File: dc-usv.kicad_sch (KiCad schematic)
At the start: 0 parts

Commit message: Partial layout
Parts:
- added CASE1: 1455L1601, Case:1455L1601, symbol Case:1455L1601
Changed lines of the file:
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@@
+    )
+  )
+  (symbol (lib_id "Case:1455L1601") (at 20.32 35.56 0) (unit 1)
+    (in_bom yes) (on_board yes) (fields_autoplaced)
+    (property "Reference" "CASE1" (id 0) (at 20.32 30.7172 0))
+    (property "Value" "1455L1601" (id 1) (at 20.32 33.2541 0))
+    (property "Footprint" "Case:1455L1601" (id 2) (at 20.32 35.56 0)
+      (effects (font (size 1.27 1.27)) hide)
+    )
+    (property "Datasheet" "https://cdn-reichelt.de/documents/datenblatt/C700/1455L1601.pdf" (id 3) (at 20.32 35.56 0)
+      (effects (font (size 1.27 1.27)) hide)
     )
   )
@@
       (reference "#PWR0216") (unit 1) (value "GND") (footprint "")
     )
-    (path "/a06395f1-7afb-45e9-b1be-eb1d60bae674/01dae7e9-d4e0-426e-b265-29ae7f554ffd"
-      (reference "#PWR0217") (unit 1) (value "+3.3V") (footprint "")
+    (path "/a06395f1-7afb-45e9-b1be-eb1d60bae674/0ccfaabc-1cfb-4d04-b197-585448db4bdb"
+      (reference "#PWR0217") (unit 1) (value "+3V3") (footprint "")
     )
     (path "/a06395f1-7afb-45e9-b1be-eb1d60bae674/9b461fb2-d53a-4d81-9704-1a7841368fff"
@@
       (reference "#PWR0296") (unit 1) (value "+3V3") (footprint "")
     )
+    (path "/a06395f1-7afb-45e9-b1be-eb1d60bae674/53a3dabf-d840-40d3-b123-be99bc0cd47b"
+      (reference "#PWR0297") (unit 1) (value "+3V3") (footprint "")
+    )
+    (path "/a06395f1-7afb-45e9-b1be-eb1d60bae674/b7e85537-781d-41e1-bbe8-d28bedf5aecc"
+      (reference "#PWR0298") (unit 1) (value "GND") (footprint "")
+    )
     (path "/a06395f1-7afb-45e9-b1be-eb1d60bae674/0ede46ea-4de7-4fa6-810f-0ba49bf63961"
-      (reference "#PWR?") (unit 1) (value "GND") (footprint "")
-    )
-    (path "/a06395f1-7afb-45e9-b1be-eb1d60bae674/53a3dabf-d840-40d3-b123-be99bc0cd47b"
-      (reference "#PWR?") (unit 1) (value "+3V3") (footprint "")
-    )
-    (path "/a06395f1-7afb-45e9-b1be-eb1d60bae674/b7e85537-781d-41e1-bbe8-d28bedf5aecc"
-      (reference "#PWR?") (unit 1) (value "GND") (footprint "")
+      (reference "#PWR0299") (unit 1) (value "GND") (footprint "")
+    )
+    (path "/9f5e79bf-a1ad-420a-9a06-1a81ab265187/9868f416-b036-4007-b8a7-93d9fd668084"
+      (reference "#PWR0300") (unit 1) (value "GND") (footprint "")
+    )
+    (path "/9f5e79bf-a1ad-420a-9a06-1a81ab265187/c7c0a035-6c4c-4ca1-80e7-b1a325e95302"
+      (reference "#PWR0301") (unit 1) (value "+3V3") (footprint "")
+    )
+    (path "/9f5e79bf-a1ad-420a-9a06-1a81ab265187/93b8629d-2dd9-48b6-a0a5-986d19c60970"
+      (reference "#PWR0302") (unit 1) (value "GND") (footprint "")
+    )
+    (path "/9f5e79bf-a1ad-420a-9a06-1a81ab265187/9e16cf65-2ec4-4650-b1d7-fd409aef4ec7"
+      (reference "#PWR0303") (unit 1) (value "GND") (footprint "")
+    )
+    (path "/9f5e79bf-a1ad-420a-9a06-1a81ab265187/289a5c1c-0bf1-4333-b01f-9d95e3fa2864"
+      (reference "#PWR0304") (unit 1) (value "GND") (footprint "")
+    )
+    (path "/a06395f1-7afb-45e9-b1be-eb1d60bae674/b2d83311-3769-443b-9605-bbef8899a620/89f70569-72d2-4912-b6e3-9703a730d568"
+      (reference "#PWR0305") (unit 1) (value "VBUS") (footprint "")
+    )
+    (path "/a06395f1-7afb-45e9-b1be-eb1d60bae674/b2d83311-3769-443b-9605-bbef8899a620/9f2c905a-ca7b-475b-8632-d31e68011e41"
+      (reference "#PWR0306") (unit 1) (value "GND") (footprint "")
     )
     (path "/aa145c2f-e167-4de3-92bf-3e0d0ae2fb67/06ec14b7-6af4-46b3-aed4-1258a100ed19"
@@
       (reference "C103") (unit 1) (value "2.2uF") (footprint "Capacitor_SMD:C_0603_1608Metric")
     )
+    (path "/9f5e79bf-a1ad-420a-9a06-1a81ab265187/88747cb4-c96e-48fe-8bd4-16f22b505b73"
+      (reference "C104") (unit 1) (value "22nF") (footprint "Capacitor_SMD:C_0402_1005Metric")
+    )
+    (path "/25526d58-38a0-4dab-a440-f8cc76091337"
+      (reference "CASE1") (unit 1) (value "1455L1601") (footprint "Case:1455L1601")
+    )
     (path "/aa145c2f-e167-4de3-92bf-3e0d0ae2fb67/defc8839-bf1e-4b04-89fc-3cffafd43258"
       (reference "D1") (unit 1) (value "1N4148WS") (footprint "Diode_SMD:D_SOD-323")
@@
       (reference "D16") (unit 1) (value "P6SMB6.8CA") (footprint "Diode_SMD:D_SMB")
     )
+    (path "/9f5e79bf-a1ad-420a-9a06-1a81ab265187/81f255d2-fff4-4286-9b04-e2b96723db7d"
+      (reference "D17") (unit 1) (value "YEL") (footprint "LED_SMD:LED_0603_1608Metric")
+    )
+    (path "/9f5e79bf-a1ad-420a-9a06-1a81ab265187/c68b69ec-7a92-49e2-b6d4-229cddc59a1a"
+      (reference "D18") (unit 1) (value "RED") (footprint "LED_SMD:LED_0603_1608Metric")
+    )
+    (path "/9f5e79bf-a1ad-420a-9a06-1a81ab265187/e64f1ef4-0563-4bae-a757-db5967d3b8e2"
+      (reference "D19") (unit 1) (value "GRN") (footprint "LED_SMD:LED_0603_1608Metric")
+    )
     (path "/aa145c2f-e167-4de3-92bf-3e0d0ae2fb67/a0a04842-0b26-4142-b5e1-0b95e4dc5d49"
       (reference "F1") (unit 1) (value "10A") (footprint "Fuse:Fuse_1206_3216Metric")
@@
       (reference "Q25") (unit 1) (value "AO3401A") (footprint "Package_TO_SOT_SMD:SOT-23")
     )
+    (path "/9f5e79bf-a1ad-420a-9a06-1a81ab265187/6c3c82b9-4c87-4dcf-ad4d-ca684d7318df"
+      (reference "Q26") (unit 1) (value "2N7002") (footprint "Package_TO_SOT_SMD:SOT-23")
+    )
     (path "/a06395f1-7afb-45e9-b1be-eb1d60bae674/b2d83311-3769-443b-9605-bbef8899a620/0b0d926e-5c20-493a-95ff-4ae891ae05a1"
       (reference "Q28") (unit 1) (value "MMBT3904") (footprint "Package_TO_SOT_SMD:SOT-23")
@@
     )
     (path "/a06395f1-7afb-45e9-b1be-eb1d60bae674/59d225b3-da12-45b8-9dfd-44678b17239f"
-      (reference "R?") (unit 1) (value "10k") (footprint "Resistor_SMD:R_0402_1005Metric")
+      (reference "R118") (unit 1) (value "10k") (footprint "Resistor_SMD:R_0402_1005Metric")
+    )
+    (path "/9f5e79bf-a1ad-420a-9a06-1a81ab265187/4a912a3f-fccf-4f23-9667-38ea759c76bf"
+      (reference "R119") (unit 1) (value "10k") (footprint "Resistor_SMD:R_0402_1005Metric")
+    )
+    (path "/9f5e79bf-a1ad-420a-9a06-1a81ab265187/f4357ab5-8e36-423b-add8-f1b628003a7c"
+      (reference "R120") (unit 1) (value "5.1k") (footprint "Resistor_SMD:R_0402_1005Metric")
+    )
+    (path "/9f5e79bf-a1ad-420a-9a06-1a81ab265187/0eca0453-18ac-4661-a9b1-51916678fe1b"
+      (reference "R121") (unit 1) (value "10k") (footprint "Resistor_SMD:R_0402_1005Metric")
     )
     (path "/4ce9e4d8-553f-40e6-a397-66d04db306f8/3152910b-dfc7-4fc7-87ab-336be9ca10d0"
@@
     )
     (path "/a06395f1-7afb-45e9-b1be-eb1d60bae674/e6846060-390f-4c53-9367-e476d0b72950"
-      (reference "SW?") (unit 1) (value "SW_Push") (footprint "Button_Switch_SMD_LCSC:x-1825027-x")
+      (reference "SW2") (unit 1) (value "SW_Push") (footprint "Button_Switch_SMD_LCSC:x-1825027-x")
     )
     (path "/aa145c2f-e167-4de3-92bf-3e0d0ae2fb67/d6dc2035-6098-4e26-82f4-b5badac60c84"
-      (reference "TH1") (unit 1) (value "10k") (footprint "Resistor_SMD:R_0805_2012Metric")
+      (reference "TH1") (unit 1) (value "10k") (footprint "Resistor_SMD:R_0402_1005Metric")
     )
     (path "/aa145c2f-e167-4de3-92bf-3e0d0ae2fb67/4006ff34-ec5f-4578-a6c2-03607b44d972"
-      (reference "TH2") (unit 1) (value "10k") (footprint "Resistor_SMD:R_0805_2012Metric")
+      (reference "TH2") (unit 1) (value "10k") (footprint "Resistor_SMD:R_0402_1005Metric")
     )
     (path "/aa145c2f-e167-4de3-92bf-3e0d0ae2fb67/287ca5de-cbb9-4736-9b09-b0aab9fee0e6"
@@
       (reference "U17") (unit 1) (value "N066-6448TSWEG03-H28") (footprint "Display_OLED:N066-6448TSWEG03-H28")
     )
+    (path "/a06395f1-7afb-45e9-b1be-eb1d60bae674/b2d83311-3769-443b-9605-bbef8899a620/3f24a504-1454-471f-9aa3-b57372c43cf7"
+      (reference "U18") (unit 1) (value "SRV05-4") (footprint "Package_TO_SOT_SMD:SOT-23-6")
+    )
     (path "/a06395f1-7afb-45e9-b1be-eb1d60bae674/b2d83311-3769-443b-9605-bbef8899a620/c8035e2e-1a39-416d-bfe6-a3df66d2a4a2"

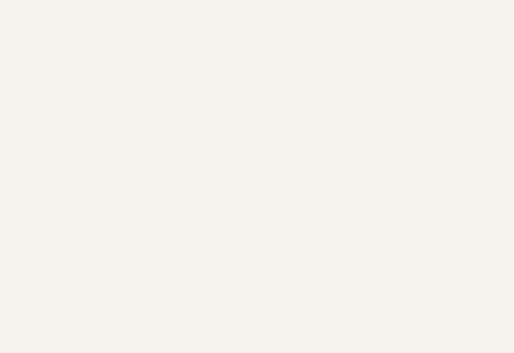
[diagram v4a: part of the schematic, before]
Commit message: Add tooling holes
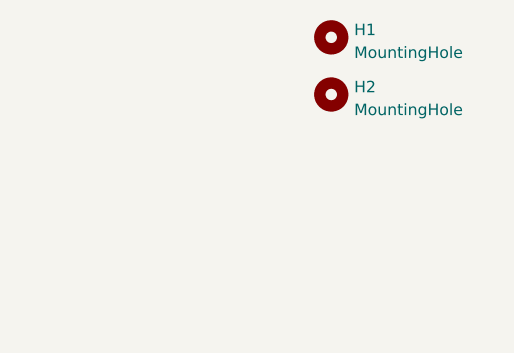
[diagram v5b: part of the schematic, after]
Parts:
- added H1, H2: MountingHole, ToolingHole:ToolingHole_JLCSMT, symbol Mechanical:MountingHole
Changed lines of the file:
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@@
+    )
+  )
+  (symbol (lib_id "Mechanical:MountingHole") (at 267.97 15.24 0) (unit 1)
+    (in_bom no) (on_board yes) (fields_autoplaced)
+    (property "Reference" "H1" (id 0) (at 270.51 14.4053 0)
+      (effects (font (size 1.27 1.27)) (justify left))
+    )
+    (property "Value" "MountingHole" (id 1) (at 270.51 16.9422 0)
+      (effects (font (size 1.27 1.27)) (justify left))
+    )
+    (property "Footprint" "ToolingHole:ToolingHole_JLCSMT" (id 2) (at 267.97 15.24 0)
+      (effects (font (size 1.27 1.27)) hide)
+    )
+    (property "Datasheet" "~" (id 3) (at 267.97 15.24 0)
+      (effects (font (size 1.27 1.27)) hide)
+    )
+  )
+  (symbol (lib_id "Mechanical:MountingHole") (at 267.97 21.59 0) (unit 1)
+    (in_bom no) (on_board yes) (fields_autoplaced)
+    (property "Reference" "H2" (id 0) (at 270.51 20.7553 0)
+      (effects (font (size 1.27 1.27)) (justify left))
+    )
+    (property "Value" "MountingHole" (id 1) (at 270.51 23.2922 0)
+      (effects (font (size 1.27 1.27)) (justify left))
+    )
+    (property "Footprint" "ToolingHole:ToolingHole_JLCSMT" (id 2) (at 267.97 21.59 0)
+      (effects (font (size 1.27 1.27)) hide)
+    )
+    (property "Datasheet" "~" (id 3) (at 267.97 21.59 0)
+      (effects (font (size 1.27 1.27)) hide)
     )
   )
@@
       (reference "F4") (unit 1) (value "5A") (footprint "Fuse:Fuse_1206_3216Metric")
     )
+    (path "/b1de0cf0-daa1-4d20-a7d3-2194d7487162"
+      (reference "H1") (unit 1) (value "MountingHole") (footprint "ToolingHole:ToolingHole_JLCSMT")
+    )
+    (path "/fdcbfa9b-5014-4601-9d27-0786e14eb279"
+      (reference "H2") (unit 1) (value "MountingHole") (footprint "ToolingHole:ToolingHole_JLCSMT")
+    )
     (path "/ba11ff08-fab3-423b-91ea-f3fea9b2bab0/c29f14bf-2136-45fb-8c2b-3167cf235adb"

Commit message: Fix footprint origins for JLC assembly
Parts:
- CASE1: now left out of the parts list
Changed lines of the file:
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@@
   )
   (symbol (lib_id "Case:1455L1601") (at 20.32 35.56 0) (unit 1)
-    (in_bom yes) (on_board yes) (fields_autoplaced)
+    (in_bom no) (on_board yes) (fields_autoplaced)
     (property "Reference" "CASE1" (id 0) (at 20.32 30.7172 0))
     (property "Value" "1455L1601" (id 1) (at 20.32 33.2541 0))
@@
       (reference "#PWR0311") (unit 1) (value "+3V3") (footprint "")
     )
+    (path "/a06395f1-7afb-45e9-b1be-eb1d60bae674/c5b7f9e4-5132-4040-87a3-40d796a53fc8"
+      (reference "#PWR0312") (unit 1) (value "GND") (footprint "")
+    )
     (path "/a06395f1-7afb-45e9-b1be-eb1d60bae674/9ac33f4a-daa8-4947-b60b-5dc5ce181da9"
-      (reference "#PWR?") (unit 1) (value "GND") (footprint "")
+      (reference "#PWR0313") (unit 1) (value "GND") (footprint "")
     )
     (path "/db902e67-672f-4e23-a96d-1719af2dd4ad/c33dcca6-4622-478c-83f2-1aea854be53c"
-      (reference "#PWR?") (unit 1) (value "GND") (footprint "")
-    )
-    (path "/a06395f1-7afb-45e9-b1be-eb1d60bae674/c5b7f9e4-5132-4040-87a3-40d796a53fc8"
-      (reference "#PWR?") (unit 1) (value "GND") (footprint "")
+      (reference "#PWR0314") (unit 1) (value "GND") (footprint "")
     )
     (path "/aa145c2f-e167-4de3-92bf-3e0d0ae2fb67/06ec14b7-6af4-46b3-aed4-1258a100ed19"
@@
     )
     (path "/a06395f1-7afb-45e9-b1be-eb1d60bae674/9a721ec3-8301-444f-9eaa-aa53e11a19f3"
-      (reference "D?") (unit 1) (value "GRN") (footprint "LED_SMD:LED_0603_1608Metric")
+      (reference "D20") (unit 1) (value "GRN") (footprint "LED_SMD:LED_0603_1608Metric")
+    )
+    (path "/a06395f1-7afb-45e9-b1be-eb1d60bae674/ba96cd70-0d01-4998-b7c4-a03709754f62"
+      (reference "D21") (unit 1) (value "YEL") (footprint "LED_SMD:LED_0603_1608Metric")
     )
     (path "/db902e67-672f-4e23-a96d-1719af2dd4ad/b9897c5f-9291-4dbc-baca-8ebe9f116bad"
-      (reference "D?") (unit 1) (value "RED") (footprint "LED_SMD:LED_0603_1608Metric")
-    )
-    (path "/a06395f1-7afb-45e9-b1be-eb1d60bae674/ba96cd70-0d01-4998-b7c4-a03709754f62"
-      (reference "D?") (unit 1) (value "YEL") (footprint "LED_SMD:LED_0603_1608Metric")
+      (reference "D22") (unit 1) (value "RED") (footprint "LED_SMD:LED_0603_1608Metric")
     )
     (path "/aa145c2f-e167-4de3-92bf-3e0d0ae2fb67/a0a04842-0b26-4142-b5e1-0b95e4dc5d49"
@@
       (reference "R123") (unit 1) (value "100R") (footprint "Resistor_SMD:R_0402_1005Metric")
     )
+    (path "/a06395f1-7afb-45e9-b1be-eb1d60bae674/c4379f97-2c10-4d7f-a19d-7b350b6eebb0"
+      (reference "R124") (unit 1) (value "5.1k") (footprint "Resistor_SMD:R_0402_1005Metric")
+    )
     (path "/a06395f1-7afb-45e9-b1be-eb1d60bae674/5fc065c3-f9e8-4f59-bdf1-9956dab5b03b"
-      (reference "R?") (unit 1) (value "5.1k") (footprint "Resistor_SMD:R_0402_1005Metric")
+      (reference "R125") (unit 1) (value "5.1k") (footprint "Resistor_SMD:R_0402_1005Metric")
     )
     (path "/db902e67-672f-4e23-a96d-1719af2dd4ad/968dbf9c-9eab-47cb-bbeb-b26c73af3685"
-      (reference "R?") (unit 1) (value "10k") (footprint "Resistor_SMD:R_0402_1005Metric")
-    )
-    (path "/a06395f1-7afb-45e9-b1be-eb1d60bae674/c4379f97-2c10-4d7f-a19d-7b350b6eebb0"
-      (reference "R?") (unit 1) (value "5.1k") (footprint "Resistor_SMD:R_0402_1005Metric")
+      (reference "R126") (unit 1) (value "10k") (footprint "Resistor_SMD:R_0402_1005Metric")
     )
     (path "/4ce9e4d8-553f-40e6-a397-66d04db306f8/3152910b-dfc7-4fc7-87ab-336be9ca10d0"
@@
     )
     (path "/a06395f1-7afb-45e9-b1be-eb1d60bae674/b2d83311-3769-443b-9605-bbef8899a620/566d4408-040e-4658-bf78-018e32d4c36a"
-      (reference "U16") (unit 1) (value "CH340G") (footprint "Package_SO:SOIC-16_3.9x9.9mm_P1.27mm")
+      (reference "U16") (unit 1) (value "CH340C") (footprint "Package_SO:SOIC-16_3.9x9.9mm_P1.27mm")
     )
     (path "/a06395f1-7afb-45e9-b1be-eb1d60bae674/09d6e4a2-a135-4aa7-a5c0-b78a7e1387c0"
@@
     )
     (path "/a06395f1-7afb-45e9-b1be-eb1d60bae674/b2d83311-3769-443b-9605-bbef8899a620/c8035e2e-1a39-416d-bfe6-a3df66d2a4a2"
-      (reference "Y1") (unit 1) (value "12MHz") (footprint "Crystal:Crystal_SMD_3225-4Pin_3.2x2.5mm")
+      (reference "Y1") (unit 1) (value "12MHz (DNP)") (footprint "Crystal:Crystal_SMD_3225-4Pin_3.2x2.5mm")
     )
   )
